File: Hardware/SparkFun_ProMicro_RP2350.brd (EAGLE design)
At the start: 17.8 x 33 mm, 118 parts, among them J2 QWIIC_RIGHT_ANGLE, J5 USB Female Type C Connector, U1 RT9080-33GJ5, U2 RP2350A, U3 WS2812_2020, U4 W25QXX128MBIT, Y1 12MHz

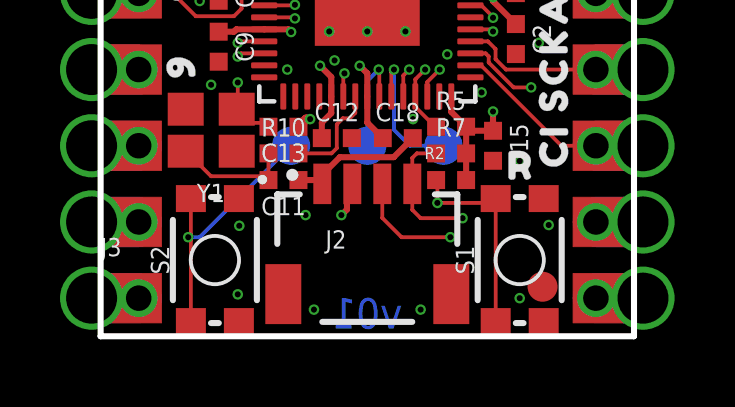
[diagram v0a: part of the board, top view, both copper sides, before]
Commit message: v10 updates
Bump version number to v10
Move bottom pin silk labels away from pads
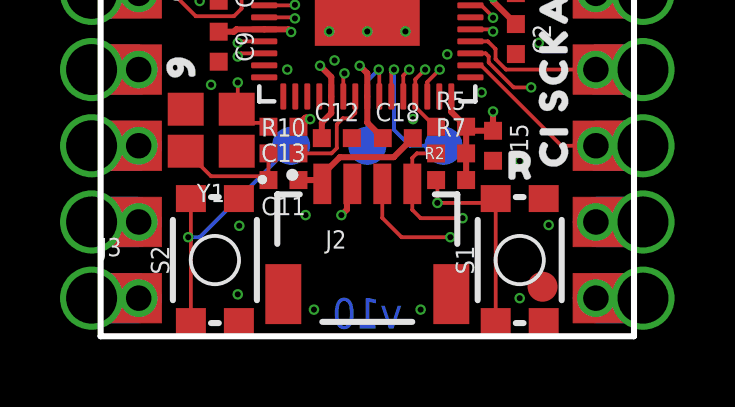
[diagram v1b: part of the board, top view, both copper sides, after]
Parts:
- moved U$19 0.64 mm to (3.17, 28.8)
- moved U$21 0.57 mm to (3.17, 26.4)
- moved U$10 0.38 mm to (13.7, 8.89)
- moved U$11 0.38 mm to (14.1, 11.4)
- moved U$12 0.38 mm to (14.2, 14.0)
- moved U$13 0.38 mm to (14.1, 16.5)
- moved U$14 0.38 mm to (14.1, 19.1)
- moved U$15 0.38 mm to (14.6, 26.7)
- moved U$66 0.25 mm to (14.1, 3.81)
- moved U$22 0.25 mm to (3.17, 22.9)
- moved U$23 0.25 mm to (2.92, 19.1)
- moved U$24 0.25 mm to (2.92, 16.5)
- moved U$25 0.25 mm to (2.92, 14.0)
- moved U$26 0.25 mm to (2.92, 11.4)
- moved U$27 0.25 mm to (2.92, 9.02)
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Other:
- board text added: "v10"
- board text removed: "v01"

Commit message: Design review updates
Re-enable layers that accidentally got turned off
Nudge BOOT and RST silk to be better centered over button art
Add better silk dot to crystal
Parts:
- moved U$41 0.13 mm to (5.59, 2.54)
- moved U$44 0.13 mm to (11.9, 2.54)
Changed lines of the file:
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@@
 <grid distance="0.05" unitdist="inch" unit="inch" style="lines" multiple="1" display="yes" altdistance="0.005" altunitdist="inch" altunit="inch"/>
 <layers>
-<layer number="1" name="Top" color="4" fill="1" visible="no" active="yes"/>
-<layer number="2" name="GND/Vert" color="23" fill="1" visible="no" active="yes"/>
-<layer number="15" name="3.3V/Horz" color="63" fill="1" visible="no" active="yes"/>
+<layer number="1" name="Top" color="4" fill="1" visible="yes" active="yes"/>
+<layer number="2" name="GND/Vert" color="23" fill="1" visible="yes" active="yes"/>
+<layer number="15" name="3.3V/Horz" color="63" fill="1" visible="yes" active="yes"/>
 <layer number="16" name="Bottom" color="1" fill="1" visible="yes" active="yes"/>
 <layer number="17" name="Pads" color="2" fill="1" visible="yes" active="yes"/>
@@
 <layer number="19" name="Unrouted" color="6" fill="1" visible="yes" active="yes"/>
 <layer number="20" name="Dimension" color="24" fill="1" visible="yes" active="yes"/>
-<layer number="21" name="tPlace" color="16" fill="1" visible="no" active="yes"/>
+<layer number="21" name="tPlace" color="16" fill="1" visible="yes" active="yes"/>
 <layer number="22" name="bPlace" color="14" fill="1" visible="yes" active="yes"/>
-<layer number="23" name="tOrigins" color="15" fill="1" visible="no" active="yes"/>
+<layer number="23" name="tOrigins" color="15" fill="1" visible="yes" active="yes"/>
 <layer number="24" name="bOrigins" color="15" fill="1" visible="yes" active="yes"/>
 <layer number="25" name="tNames" color="7" fill="1" visible="no" active="yes"/>
@@
 <layer number="37" name="tTest" color="7" fill="1" visible="no" active="yes"/>
 <layer number="38" name="bTest" color="7" fill="1" visible="no" active="yes"/>
-<layer number="39" name="tKeepout" color="4" fill="11" visible="no" active="yes"/>
+<layer number="39" name="tKeepout" color="4" fill="11" visible="yes" active="yes"/>
 <layer number="40" name="bKeepout" color="1" fill="11" visible="yes" active="yes"/>
-<layer number="41" name="tRestrict" color="4" fill="10" visible="no" active="yes"/>
+<layer number="41" name="tRestrict" color="4" fill="10" visible="yes" active="yes"/>
 <layer number="42" name="bRestrict" color="1" fill="10" visible="yes" active="yes"/>
 <layer number="43" name="vRestrict" color="2" fill="10" visible="yes" active="yes"/>
@@
 <layer number="49" name="Reference" color="13" fill="1" visible="yes" active="yes"/>
 <layer number="50" name="dxf" color="7" fill="1" visible="no" active="yes"/>
-<layer number="51" name="tDocu" color="6" fill="1" visible="no" active="yes"/>
+<layer number="51" name="tDocu" color="6" fill="1" visible="yes" active="yes"/>
 <layer number="52" name="bDocu" color="7" fill="1" visible="yes" active="yes"/>
 <layer number="91" name="Nets" color="2" fill="1" visible="no" active="no"/>
@@
 <circle x="6.223" y="0.762" radius="0.127" width="0.1524" layer="22"/>
 <circle x="5.207" y="0.762" radius="0.127" width="0.1524" layer="22"/>
+<circle x="4.894" y="5.318" radius="0.161553125" width="0" layer="21"/>
 </plain>
 <attributes>
@@
 <element name="U$43" library="output" package="#SHLD#0" value="" x="11.43" y="25.146" smashed="yes" rot="MR270"/>
 <element name="U$36" library="output" package="#P#0" value="" x="3.302" y="30.353" smashed="yes" rot="MR0"/>
-<element name="U$41" library="output" package="BOOT0" value="" x="5.715" y="2.54" smashed="yes" rot="MR0"/>
-<element name="U$44" library="output" package="RST0" value="" x="12.065" y="2.54" smashed="yes" rot="MR0"/>
+<element name="U$41" library="output" package="BOOT0" value="" x="5.588" y="2.54" smashed="yes" rot="MR0"/>
+<element name="U$44" library="output" package="RST0" value="" x="11.938" y="2.54" smashed="yes" rot="MR0"/>
 </elements>
 <signals>

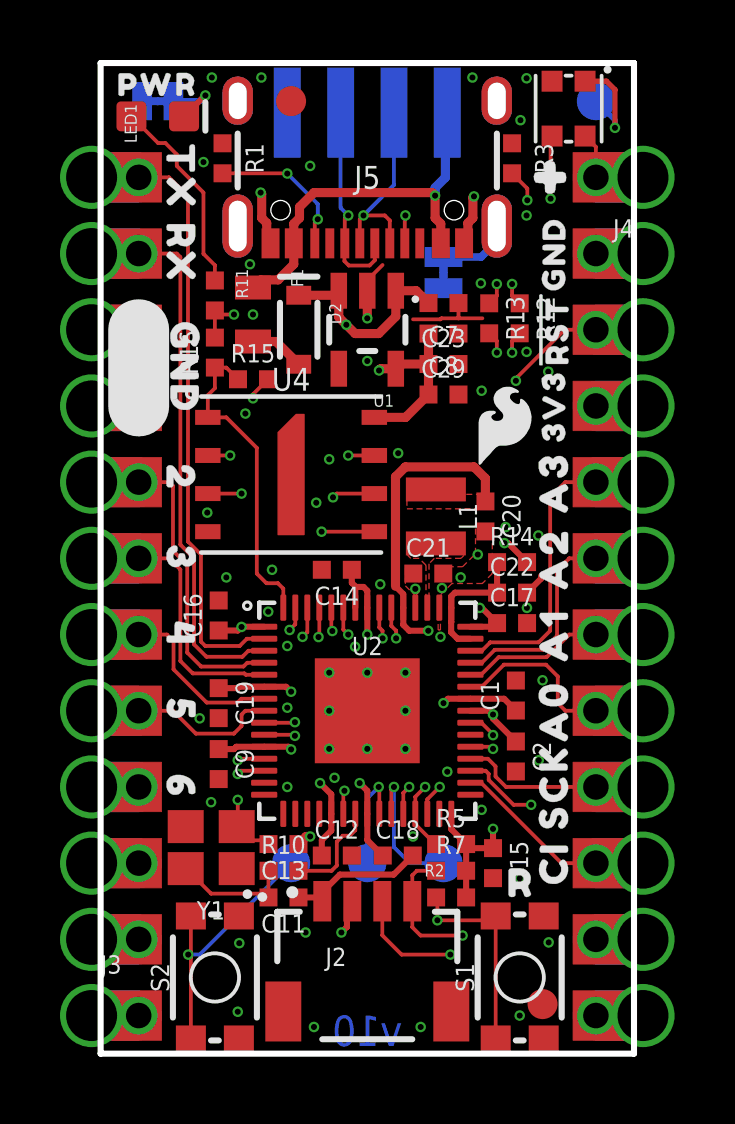
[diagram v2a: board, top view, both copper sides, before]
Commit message: Add PSRAM
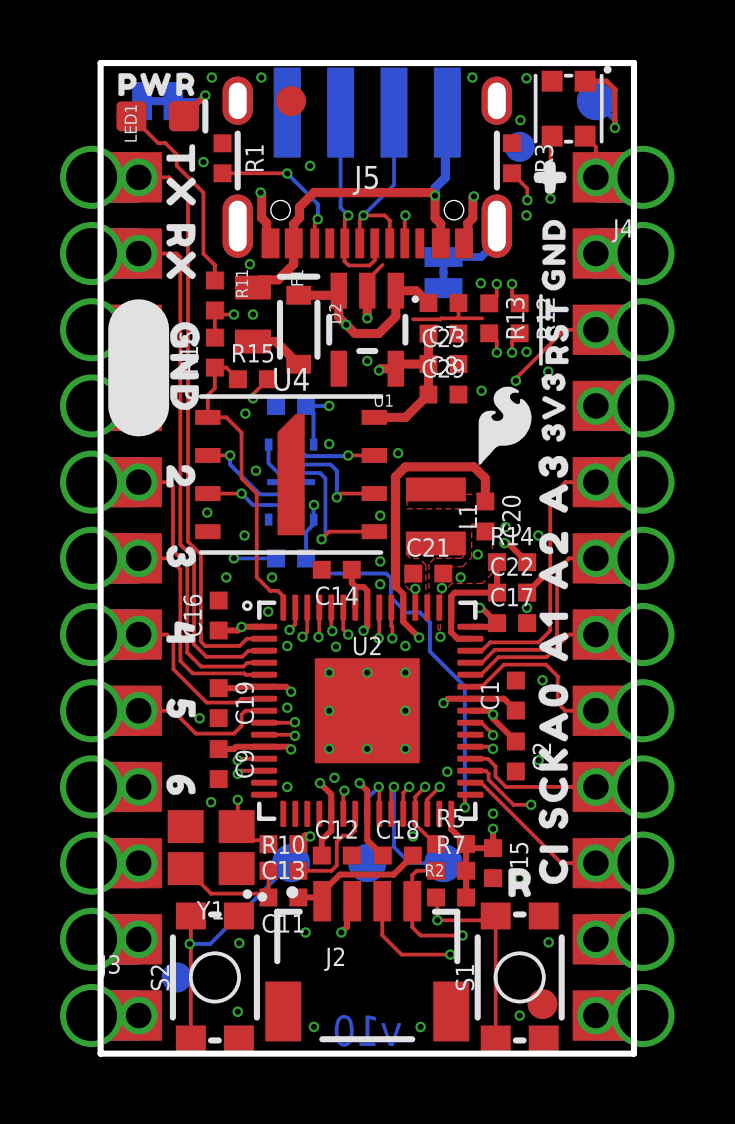
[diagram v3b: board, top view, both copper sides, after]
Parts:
- added C3: 0.1uF, SparkFun-Capacitors:0402-TIGHT
- added JP3, JP4: FIDUCIAL1X2, SparkFun-Aesthetics:FIDUCIAL-1X2
- added R4: 10k, SparkFun-Resistors:0402-TIGHT
- added U5: APS6404L-3SQR-ZR, RP2350A:APS6404L-3SQR-ZR
- moved LOGO1 1.80 mm to (8.89, 15.2)
- moved U$4 1.63 mm to (10.7, 13.5)
- moved U$42 1.08 mm to (12.2, 13.6)
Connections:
- net QSPI-CS renamed FLASH_!CS!/BOOT
- new net PSRAM_!CS!: R4.1, U2.31, U5.1
- net 3.3V: now also C3.1, R4.2, U5.8
- net GND: now also C3.2, U5.4, U5.9
- net QSPI-0: now also U5.5
- net QSPI-1: now also U5.2
- net QSPI-2: now also U5.3
- net QSPI-3: now also U5.7
- net QSPI-CLK: now also U5.6
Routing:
- net PSRAM_!CS!: track 0.00 -> 14.5 mm, vias 0 -> 2
- net QSPI-0: track 6.30 -> 11.0 mm
- net QSPI-1: track 8.38 -> 12.0 mm
- net 3.3V: track 29.6 -> 33.1 mm, vias 12 -> 14
- net QSPI-CLK: track 6.69 -> 9.85 mm
- net QSPI-2: track 7.92 -> 9.88 mm
- net QSPI-3: track 7.80 -> 9.70 mm
- net BOOT: track 29.5 -> 28.9 mm
- net GND: vias 63 -> 67

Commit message: Change version number to v09
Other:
- board text added: "v09"
- board text removed: "v10"
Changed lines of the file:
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@@
 <wire x1="17.78" y1="0" x2="17.78" y2="33.02" width="0.2032" layer="20"/>
 <wire x1="17.78" y1="33.02" x2="0" y2="33.02" width="0.2032" layer="20"/>
-<text x="8.89" y="0.762" size="1.016" layer="16" font="vector" ratio="25" rot="MR0" align="center">v10</text>
+<text x="8.89" y="0.762" size="1.016" layer="16" font="vector" ratio="25" rot="MR0" align="center">v09</text>
 <wire x1="1.27" y1="24.13" x2="1.27" y2="21.59" width="2.032" layer="21"/>
 <wire x1="1.27" y1="24.13" x2="1.27" y2="21.59" width="2.032" layer="22"/>
@@
 <element name="FRAME2" library="SparkFun-Aesthetics" package="CREATIVE_COMMONS" value="FRAME-LEDGER" x="39.37" y="-7.62" smashed="yes">
 <attribute name="DESIGNER" value="Dryw Wade" x="39.37" y="-7.62" size="1.778" layer="27" font="vector" ratio="15" display="off"/>
-<attribute name="REV" value="v10" x="39.37" y="-7.62" size="1.778" layer="27" font="vector" ratio="15" display="off"/>
+<attribute name="REV" value="v09" x="39.37" y="-7.62" size="1.778" layer="27" font="vector" ratio="15" display="off"/>
 </element>
 <element name="U$4" library="output" package="PRO_MICRO0" value="" x="10.668" y="13.462" smashed="yes" rot="MR270"/>

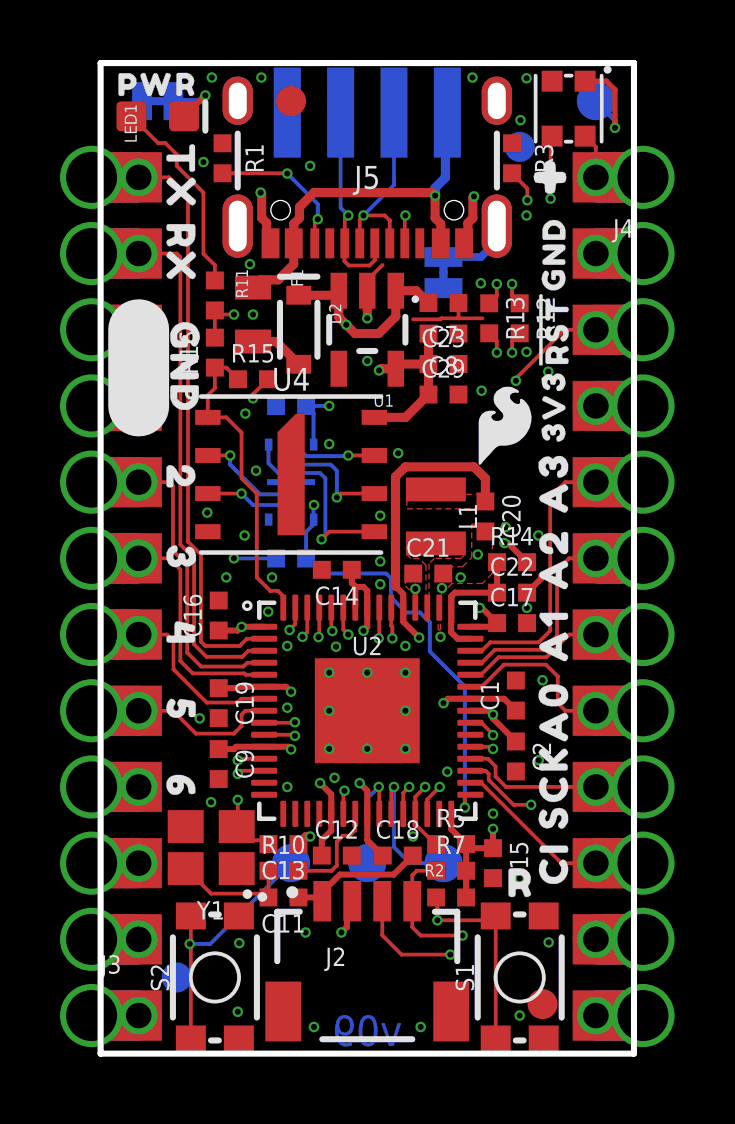
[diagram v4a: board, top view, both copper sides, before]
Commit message: Move power components to bottom
Gives more clearance between components to hopefully improve production yields
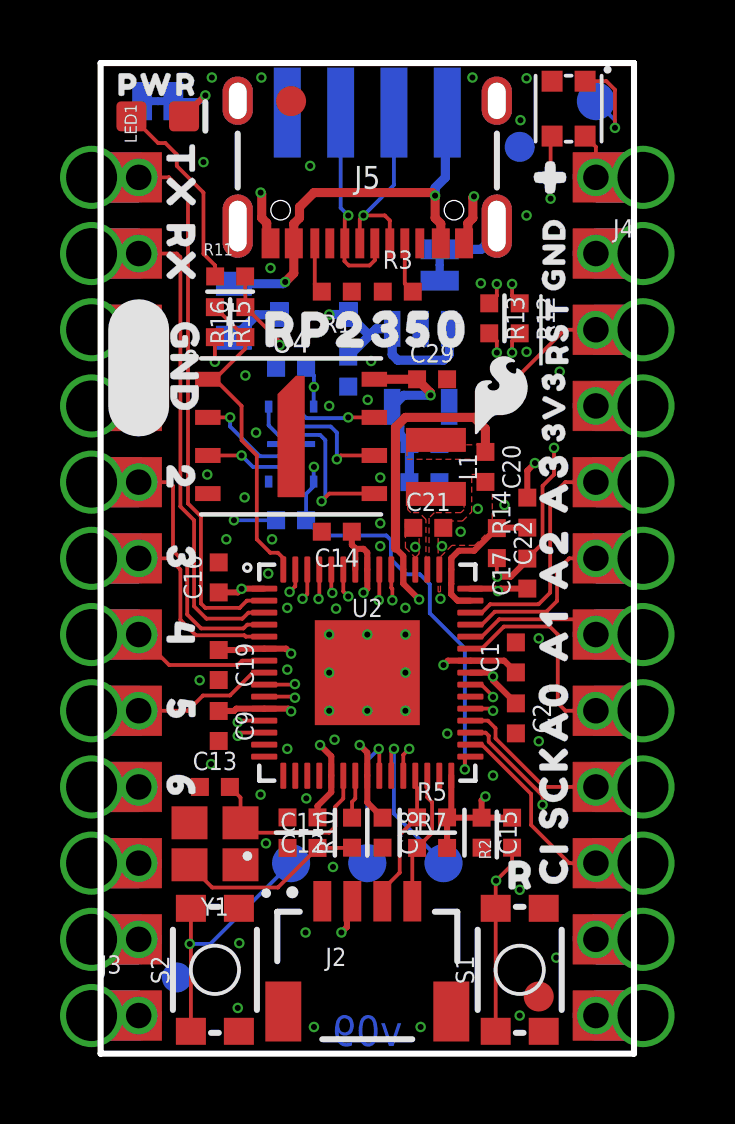
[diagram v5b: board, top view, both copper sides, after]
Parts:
- added U$45: (no value), output:RP23500
- moved R1 5.85 mm to (7.87, 25.4), turned to 180 degrees
- moved R3 5.85 mm to (9.91, 25.4), turned to 0 degrees
- moved U$3 4.49 mm to (5.08, 14.6)
- moved C23 3.99 mm to (10.8, 19.1), flipped to the bottom, turned to 180 degrees
- moved C7 3.91 mm to (8.26, 22.7), flipped to the bottom, turned to 90 degrees
- moved C8 3.74 mm to (10.8, 20.3), flipped to the bottom, turned to 0 degrees
- moved C13 2.98 mm to (3.81, 8.89), turned to 0 degrees
- moved R2 2.96 mm to (13.7, 7.37), turned to 90 degrees
- moved R10 2.62 mm to (8.38, 7.37), turned to 90 degrees
- moved R15 2.29 mm to (3.81, 24.4), turned to 270 degrees
- moved U1 2.18 mm to (10.7, 22.9), flipped to the bottom
- moved C11 1.77 mm to (6.73, 6.86), turned to 0 degrees
- moved R14 1.73 mm to (14.2, 18.0), turned to 90 degrees
- moved C22 1.73 mm to (13.2, 17.0), turned to 270 degrees
- moved C17 1.73 mm to (14.2, 16.0), turned to 90 degrees
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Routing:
- net 16/SDA: track 12.0 -> 4.69 mm, vias 2 -> 0
- net 17/SCL: track 10.7 -> 4.62 mm, vias 2 -> 0
- net N$9: track 7.29 -> 1.72 mm, vias 2 -> 0
- net GND: track 14.3 -> 9.50 mm
- net N$10: track 4.95 -> 1.71 mm, vias 2 -> 0
- net X1B: track 3.99 -> 6.28 mm
- net 3.3V: track 33.1 -> 35.3 mm
- net X1A: track 3.47 -> 1.44 mm
- net A0: track 7.22 -> 8.56 mm
- net 3: track 9.15 -> 7.82 mm
- net 1/RX0: track 18.7 -> 17.4 mm
- net 0/TX0: track 20.8 -> 19.5 mm
- net A3: track 10.7 -> 9.42 mm
- net 9/RX1: track 13.2 -> 14.5 mm
- net 8/TX1: track 10.6 -> 11.9 mm
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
